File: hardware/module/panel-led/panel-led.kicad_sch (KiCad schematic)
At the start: 2 parts

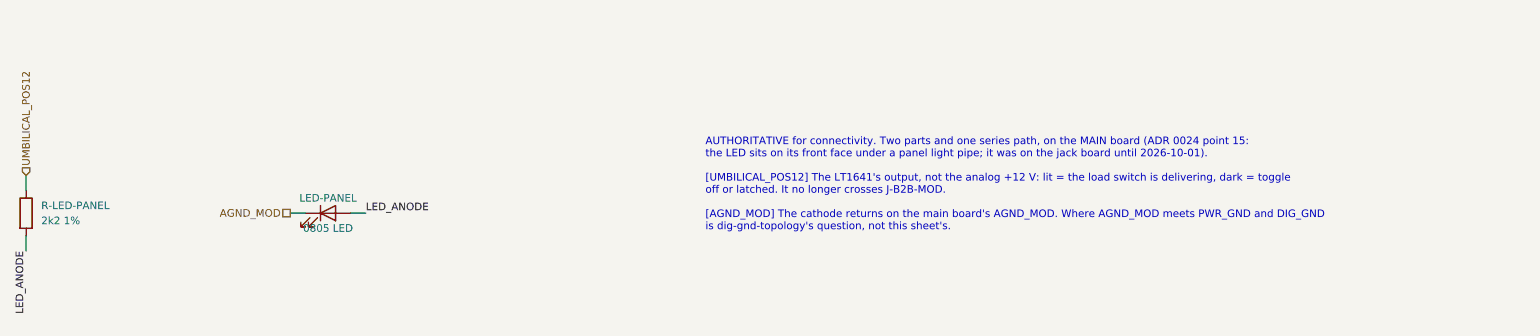
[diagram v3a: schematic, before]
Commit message: Panel LED: a panel-mount indicator wired to a header on module-main, replacing the light pipe (CAD, config, sheet)
LED-PANEL becomes a Dialight 605-2211-110F in a D5.2 panel hole; J-LED-PANEL (JST B2B-XH-A)
on the main board's front face takes its lead. Module CAD rebuilt except the Blender photos:
DRC 0 FAIL, clash 0. panel-led sheet exported and rendered; module-main re-exported.

Co-Authored-By: Claude Opus 5.5 <noreply@anthropic.com>
Claude-Session: https://claude.ai/code/session_01LmB4muFXnoLprWX4JzuJ5A
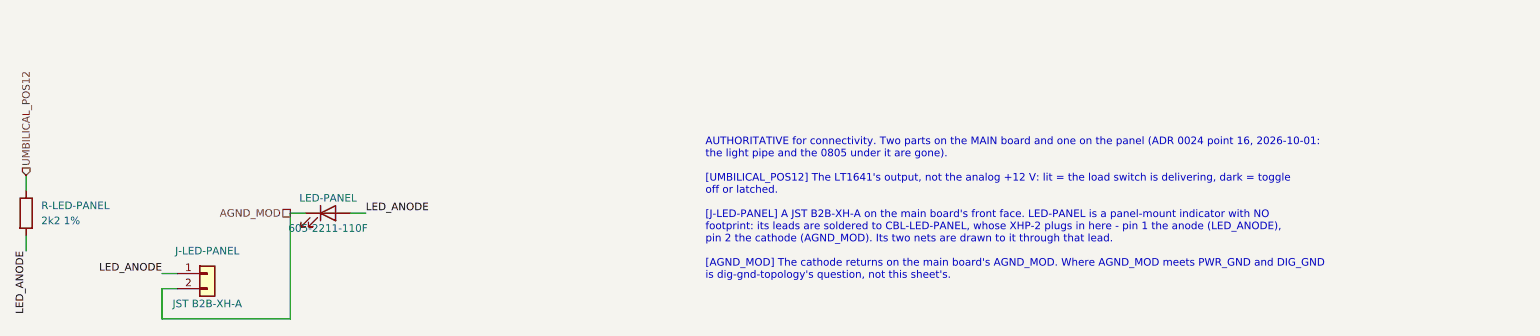
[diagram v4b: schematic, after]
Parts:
- added J-LED-PANEL: JST B2B-XH-A, Connector_JST:JST_XH_B2B-XH-A_1x02_P2.50mm_Vertical, symbol Connector_Generic:Conn_01x02
- LED-PANEL: value 0805 LED -> 605-2211-110F; footprint LED_SMD:LED_0805_2012Metric -> (none); Assembly machine -> hand; LCSC C913075 -> (none); MPN LTST-C171GKT -> 605-2211-110F; Manufacturer Lite-On -> Dialight; Note LIT = THE LOAD SWITCH IS DELIVERING. It hangs on UMBILICAL_POS12, the LT1641 output, so it is dark with the toggle off and dark when the -1 has latched on a fault - the one indication the latching design needs. It does not say the instrument is plugged in. On the MAIN board's front face, under MECH-LED-BEZEL-MOD, the panel light pipe (ADR 0024 point 15) -> LIT = THE LOAD SWITCH IS DELIVERING. It hangs on UMBILICAL_POS12, the LT1641 output, so it is dark with the toggle off and dark when the -1 has latched on a fault - the one indication the latching design needs. It does not say the instrument is plugged in. PANEL-MOUNTED (ADR 0024 point 16): no footprint on the board - its leads are cut short and soldered to CBL-LED-PANEL, the lead that plugs into J-LED-PANEL, anode to pin 1; Pins_source datasheets/led/LITEON-LTST-C171GKT-0805-GREEN.pdf p.1: the 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 -> datasheets/led/DIALIGHT-605-SERIES-PMI-CATALOG-2021-EXCERPT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
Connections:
- net AGND_MOD: now also J-LED-PANEL.2 (Pin_2)
- net LED_ANODE: now also J-LED-PANEL.1 (Pin_1)
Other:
- note added: "AUTHORITATIVE for connectivity. Two parts on the MAIN board and one on the panel (ADR 0024 point 16, 2026-10-01: the light pipe and the 0805 under it are gone). [UMBILICAL_POS12] The LT1641's output, not the analog +12 V: lit = the load switch is delivering, dark = toggle off or latched. [J-LED-PANEL] A JST B2B-XH-A on the main board's front face. LED-PANEL is a panel-mount indicator with NO foot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"
- note removed: "AUTHORITATIVE for connectivity. Two parts and one series path, on the MAIN board (ADR 0024 point 15: the LED sits on its front face under a panel light pipe; it was on the jack board until 2026-10-01). [UMBILICAL_POS12] The LT1641's output, not the analog +12 V: lit = the load switch is delivering, dark = toggle off or latched. It no longer crosses J-B2B-MOD. [AGND_MOD] The cathode returns on the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"
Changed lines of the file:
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@@
     (comment 2 "Part facts ride on each symbol: Row (BOM row), Pins + Pins_source (pin map and its datasheet), Note")
     (comment 3 "ADR 0004, ADR 0019 - migrated from its hand-written netlist.yaml, compared part by part and net by net")
-    (comment 4 "Ports are hierarchical labels (Dir, From/To, Figure); the module jack board places this sheet")
+    (comment 4 "Ports are hierarchical labels (Dir, From/To, Figure); the module main board places this sheet")
   )
   (symbol (lib_id "Device:R") (at 40.64 50.8 0) (unit 1)
@@
     (in_bom yes) (on_board yes) (dnp no)
     (property "Reference" "LED-PANEL" (at 91.44 48.26 0) (effects (font (size 1.27 1.27))))
-    (property "Value" "0805 LED" (at 91.44 53.34 0) (effects (font (size 1.27 1.27))))
-    (property "Footprint" "LED_SMD:LED_0805_2012Metric" (at 91.44 50.8 0) (effects (font (size 1.27 1.27)) hide))
+    (property "Value" "605-2211-110F" (at 91.44 53.34 0) (effects (font (size 1.27 1.27))))
+    (property "Footprint" "" (at 91.44 50.8 0) (effects (font (size 1.27 1.27)) hide))
     (property "Datasheet" "" (at 91.44 50.8 0) (effects (font (size 1.27 1.27)) hide))
     (property "Row" "LED-PANEL" (at 91.44 50.8 0) (effects (font (size 1.27 1.27)) hide))
     (property "Pins" "A=2(A) K=1(K)" (at 91.44 50.8 0) (effects (font (size 1.27 1.27)) hide))
-    (property "Note" "LIT = THE LOAD SWITCH IS DELIVERING. It hangs on UMBILICAL_POS12, the LT1641 output, so it is dark with the toggle off and dark when the -1 has latched on a fault - the one indication the latching design needs. It does not say the instrument is plugged in. On the MAIN board's front face, under MECH-LED-BEZEL-MOD, the panel light pipe (ADR 0024 point 15)" (at 91.44 50.8 0) (effects (font (size 1.27 1.27)) hide))
-    (property "Pins_source" "datasheets/led/LITEON-LTST-C171GKT-0805-GREEN.pdf p.1: the cathode is the end the package drawing marks CATHODE (the polarity bar); KiCad's LED_0805_2012Metric pad 1 is the cathode" (at 91.44 50.8 0) (effects (font (size 1.27 1.27)) hide))
-    (property "Manufacturer" "Lite-On" (at 91.44 50.8 0) (effects (font (size 1.27 1.27)) hide))
-    (property "MPN" "LTST-C171GKT" (at 91.44 50.8 0) (effects (font (size 1.27 1.27)) hide))
-    (property "LCSC" "C913075" (at 91.44 50.8 0) (effects (font (size 1.27 1.27)) hide))
-    (property "Assembly" "machine" (at 91.44 50.8 0) (effects (font (size 1.27 1.27)) hide))
+    (property "Note" "LIT = THE LOAD SWITCH IS DELIVERING. It hangs on UMBILICAL_POS12, the LT1641 output, so it is dark with the toggle off and dark when the -1 has latched on a fault - the one indication the latching design needs. It does not say the instrument is plugged in. PANEL-MOUNTED (ADR 0024 point 16): no footprint on the board - its leads are cut short and soldered to CBL-LED-PANEL, the lead that plugs into J-LED-PANEL, anode to pin 1" (at 91.44 50.8 0) (effects (font (size 1.27 1.27)) hide))
+    (property "Pins_source" "datasheets/led/DIALIGHT-605-SERIES-PMI-CATALOG-2021-EXCERPT.pdf p.1: 'Anode (Dot)' - the anode lead is the one the dot on the housing's back marks. A stand-in pin map: the LED is on the panel, and its pins are its two leads as the lead reaches them" (at 91.44 50.8 0) (effects (font (size 1.27 1.27)) hide))
+    (property "Manufacturer" "Dialight" (at 91.44 50.8 0) (effects (font (size 1.27 1.27)) hide))
+    (property "MPN" "605-2211-110F" (at 91.44 50.8 0) (effects (font (size 1.27 1.27)) hide))
+    (property "LCSC" "" (at 91.44 50.8 0) (effects (font (size 1.27 1.27)) hide))
+    (property "Assembly" "hand" (at 91.44 50.8 0) (effects (font (size 1.27 1.27)) hide))
     (pin "1")
     (pin "2")
     (instances (project "module-main" (path "/fc77e9f9-9171-5c83-92ae-8cafe880764e/00556410-138e-4c9b-bcc3-1c0a26b76f50" (reference "D16") (unit 1))) (project "panel-led" (path "/5869b789-0aae-533b-a7bd-19d896fa22ed" (reference "LED-PANEL") (unit 1))))
+  )
+  (symbol (lib_id "Connector_Generic:Conn_01x02") (at 71.12 60.96 0) (unit 1)
+    (in_bom yes) (on_board yes) (dnp no)
+    (property "Reference" "J-LED-PANEL" (at 71.12 57.15 0) (effects (font (size 1.27 1.27))))
+    (property "Value" "JST B2B-XH-A" (at 71.12 66.04 0) (effects (font (size 1.27 1.27))))
+    (property "Footprint" "Connector_JST:JST_XH_B2B-XH-A_1x02_P2.50mm_Vertical" (at 71.12 60.96 0) (effects (font (size 1.27 1.27)) hide))
+    (property "Datasheet" "" (at 71.12 60.96 0) (effects (font (size 1.27 1.27)) hide))
+    (property "Row" "J-LED-PANEL" (at 71.12 60.96 0) (effects (font (size 1.27 1.27)) hide))
+    (property "Pins" "1=1 2=2" (at 71.12 60.96 0) (effects (font (size 1.27 1.27)) hide))
+    (property "Note" "LED-PANEL's lead plugs in here (ADR 0024 point 16): pin 1 = LED_ANODE (the anode, the red wire), pin 2 = AGND_MOD (the cathode). Polarised by its shroud; mark pin 1 and A on the silk. On the main board's FRONT face, top entry, below the LED (mechanical/module/export/pcb-geometry.echo 'J-LED-PANEL')" (at 71.12 60.96 0) (effects (font (size 1.27 1.27)) hide))
+    (property "Pins_source" "datasheets/connectors/JST-XH-SERIES.pdf p.3: B2B-XH-A, circuit No.1 marked on the shroud; KiCad's JST_XH_B2B-XH-A_1x02_P2.50mm_Vertical pad 1 is circuit 1" (at 71.12 60.96 0) (effects (font (size 1.27 1.27)) hide))
+    (property "Manufacturer" "JST" (at 71.12 60.96 0) (effects (font (size 1.27 1.27)) hide))
+    (property "MPN" "B2B-XH-A(LF)(SN)" (at 71.12 60.96 0) (effects (font (size 1.27 1.27)) hide))
+    (property "LCSC" "C158012" (at 71.12 60.96 0) (effects (font (size 1.27 1.27)) hide))
+    (property "Assembly" "hand" (at 71.12 60.96 0) (effects (font (size 1.27 1.27)) hide))
+    (pin "1")
+    (pin "2")
+    (instances (project "module-main" (path "/fc77e9f9-9171-5c83-92ae-8cafe880764e/00556410-138e-4c9b-bcc3-1c0a26b76f50" (reference "J4") (unit 1))) (project "panel-led" (path "/5869b789-0aae-533b-a7bd-19d896fa22ed" (reference "J-LED-PANEL") (unit 1))))
   )
   (wire (pts (xy 40.64 46.99) (xy 40.64 44.45)) (stroke (width 0) (type default)))
@@
     (property "From" "module/power-entry" (at 85.09 50.8 0) (effects (font (size 1.27 1.27)) hide))
     (property "Figure" "dig-gnd-topology" (at 85.09 50.8 0) (effects (font (size 1.27 1.27)) hide)))
-  (text "AUTHORITATIVE for connectivity. Two parts and one series path, on the MAIN board (ADR 0024 point 15:\nthe LED sits on its front face under a panel light pipe; it was on the jack board until 2026-10-01).\n\n[UMBILICAL_POS12] The LT1641's output, not the analog +12 V: lit = the load switch is delivering, dark = toggle\noff or latched. It no longer crosses J-B2B-MOD.\n\n[AGND_MOD] The cathode returns on the main board's AGND_MOD. Where AGND_MOD meets PWR_GND and DIG_GND\nis dig-gnd-topology's question, not this sheet's." (at 154.94 38.099999999999994 0) (effects (font (size 1.27 1.27)) (justify left top)))
+  (wire (pts (xy 66.04 60.96) (xy 63.5 60.96)) (stroke (width 0) (type default)))
+  (label "LED_ANODE" (at 63.5 60.96 180) (fields_autoplaced) (effects (font (size 1.27 1.27)) (justify right bottom)))
+  (wire (pts (xy 66.04 63.5) (xy 63.5 63.5)) (stroke (width 0) (type default)))
+  (wire (pts (xy 63.5 63.5) (xy 63.5 68.58)) (stroke (width 0) (type default)))
+  (wire (pts (xy 63.5 68.58) (xy 85.09 68.58)) (stroke (width 0) (type default)))
+  (wire (pts (xy 85.09 68.58) (xy 85.09 50.8)) (stroke (width 0) (type default)))
+  (text "AUTHORITATIVE for connectivity. Two parts on the MAIN board and one on the panel (ADR 0024 point 16, 2026-10-01:\nthe light pipe and the 0805 under it are gone).\n\n[UMBILICAL_POS12] The LT1641's output, not the analog +12 V: lit = the load switch is delivering, dark = toggle\noff or latched.\n\n[J-LED-PANEL] A JST B2B-XH-A on the main board's front face. LED-PANEL is a panel-mount indicator with NO\nfootprint: its leads are soldered to CBL-LED-PANEL, whose XHP-2 plugs in here - pin 1 the anode (LED_ANODE),\npin 2 the cathode (AGND_MOD). Its two nets are drawn to it through that lead.\n\n[AGND_MOD] The cathode returns on the main board's AGND_MOD. Where AGND_MOD meets PWR_GND and DIG_GND\nis dig-gnd-topology's question, not this sheet's." (at 154.94 38.099999999999994 0) (effects (font (size 1.27 1.27)) (justify left top)))
   (sheet_instances (path "/" (page "1")))
 )
